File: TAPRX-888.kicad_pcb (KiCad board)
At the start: 6 copper layers, 83.5 x 99.4 mm, 225 parts, among them J1 CONN_SMA_JACK_EDGE_JLC_With_N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, J10 U.FL-R, J11 Conn_JTAG10-mini, J2 CONN_SMA_JACK_EDGE_JLC_With_N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, J3 CONN_SMA_JACK_EDGE_JLC_With_N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, J4 CONN_SMA_JACK_EDGE_JLC_With_N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, J5 USB-3.0, J6 Conn_01x03, J7 Conn_01x03, J8 Conn_01x03, J9 Conn_01x03, Q1 PMOS Si2343DS, Q2 MMBT3904, Q3 PMOS Si2343DS, U1 AP2114H-3.3TRG1, U10 XO-19.2MHZ, U11 CYUSB3014-BZXCT, U12 BAV99, U13 BAV99, U14 LP5907MFX-3.3, U15 BAV99, U16 TLV3501, U17 BAV99, U18 NC7SV157, U19 74LVC2G14, U2 AP2114H-3.3TRG1, U20 Si5351A, U21 NC7SV157, U22 SN65LVDS1, U3 AP2114H-3.3TRG1, U4 LP5907MFX-3.3, U5 UMW AMS1117-1.2, U6 AD8370, U7 TVS-SP3011, U8 LTC2208CUP#PBF, U9 MX25L3233FM2I, X1 TCXO-27M

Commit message: USB2/3 tweaks pt.3
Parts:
- moved C39 1.08 mm to (156.2, 74.1)
- moved C40 1.08 mm to (155.0, 74.1)
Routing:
- net /SSTX+: track 12.0 -> 13.2 mm
- net /FX3_SSTX+: track 2.97 -> 2.38 mm
- net /SSRX+: track 15.4 -> 14.8 mm
- net /SSTX-: track 12.3 -> 12.8 mm

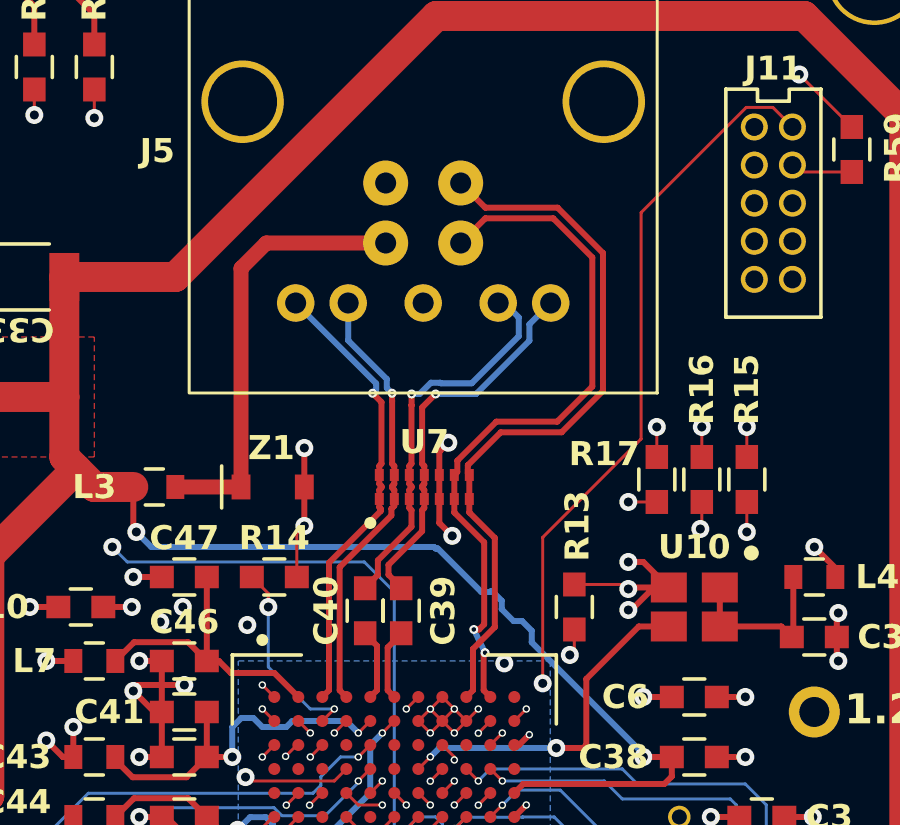
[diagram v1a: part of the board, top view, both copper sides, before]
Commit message: USB2/3 diff designs rules and PCB design passing them complete
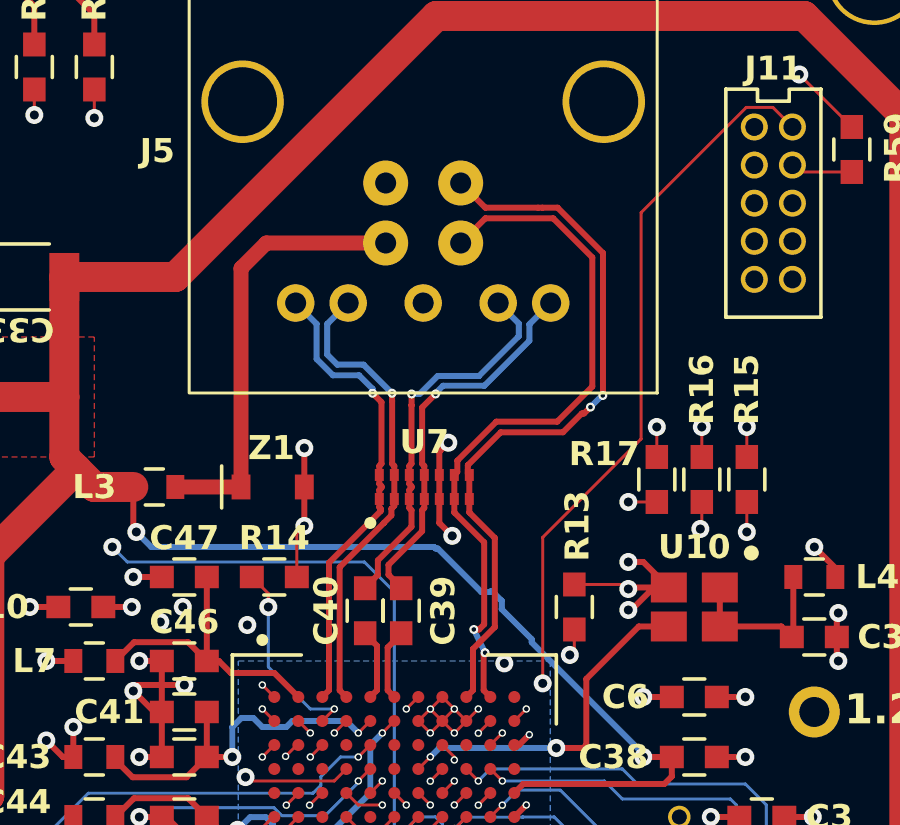
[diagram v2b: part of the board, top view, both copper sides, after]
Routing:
- net /SSRX+: track 14.8 -> 15.8 mm
- net /USB+: track 24.3 -> 24.4 mm, vias 0 -> 2
